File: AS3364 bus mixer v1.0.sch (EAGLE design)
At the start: 93 parts, among them IC1 TL072JT, IC2 TL072JT, IC3 TL072JT, IC30 TL072JT, IC4 TL072JT, IC5 79L09F, IC6 78L09F, IC7 CH446Q

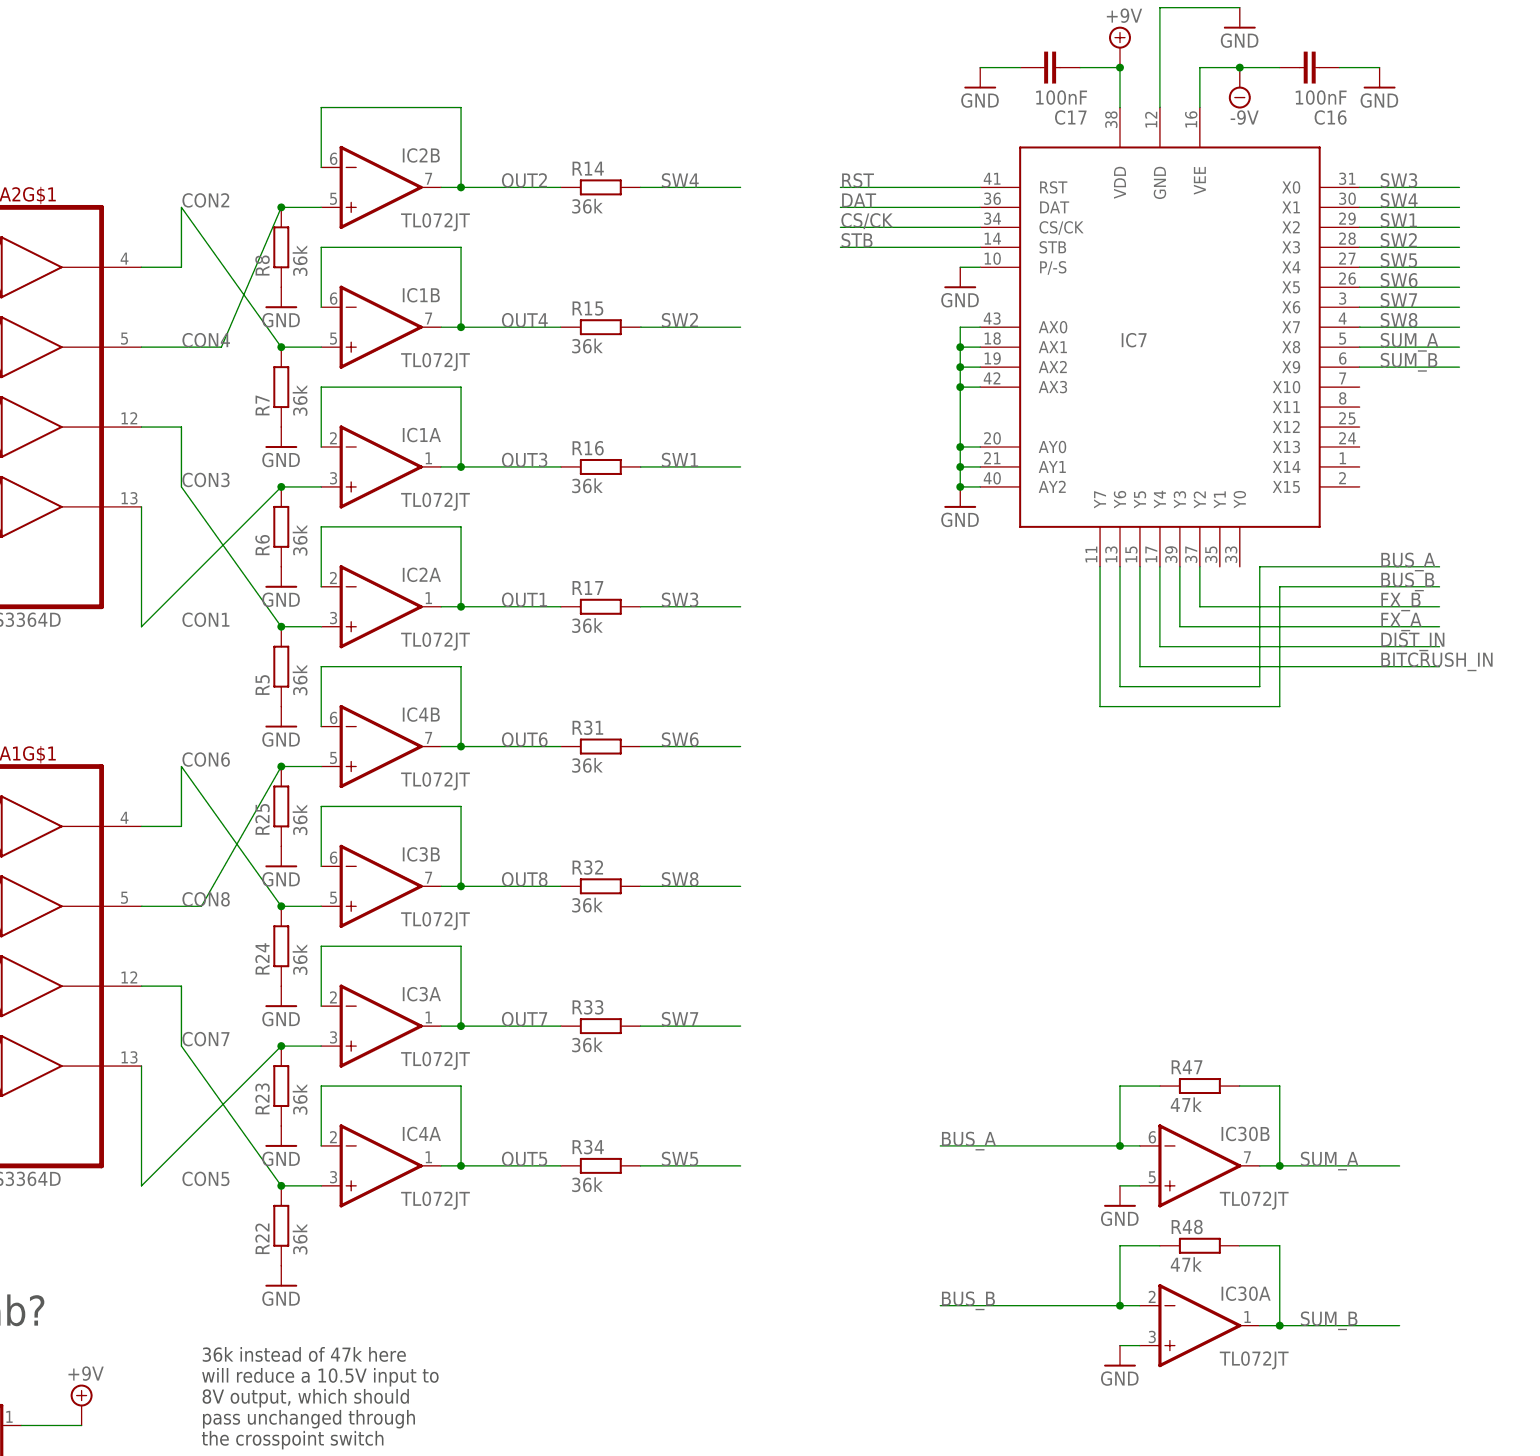
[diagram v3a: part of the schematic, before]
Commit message: Reordered lines to make coding easier
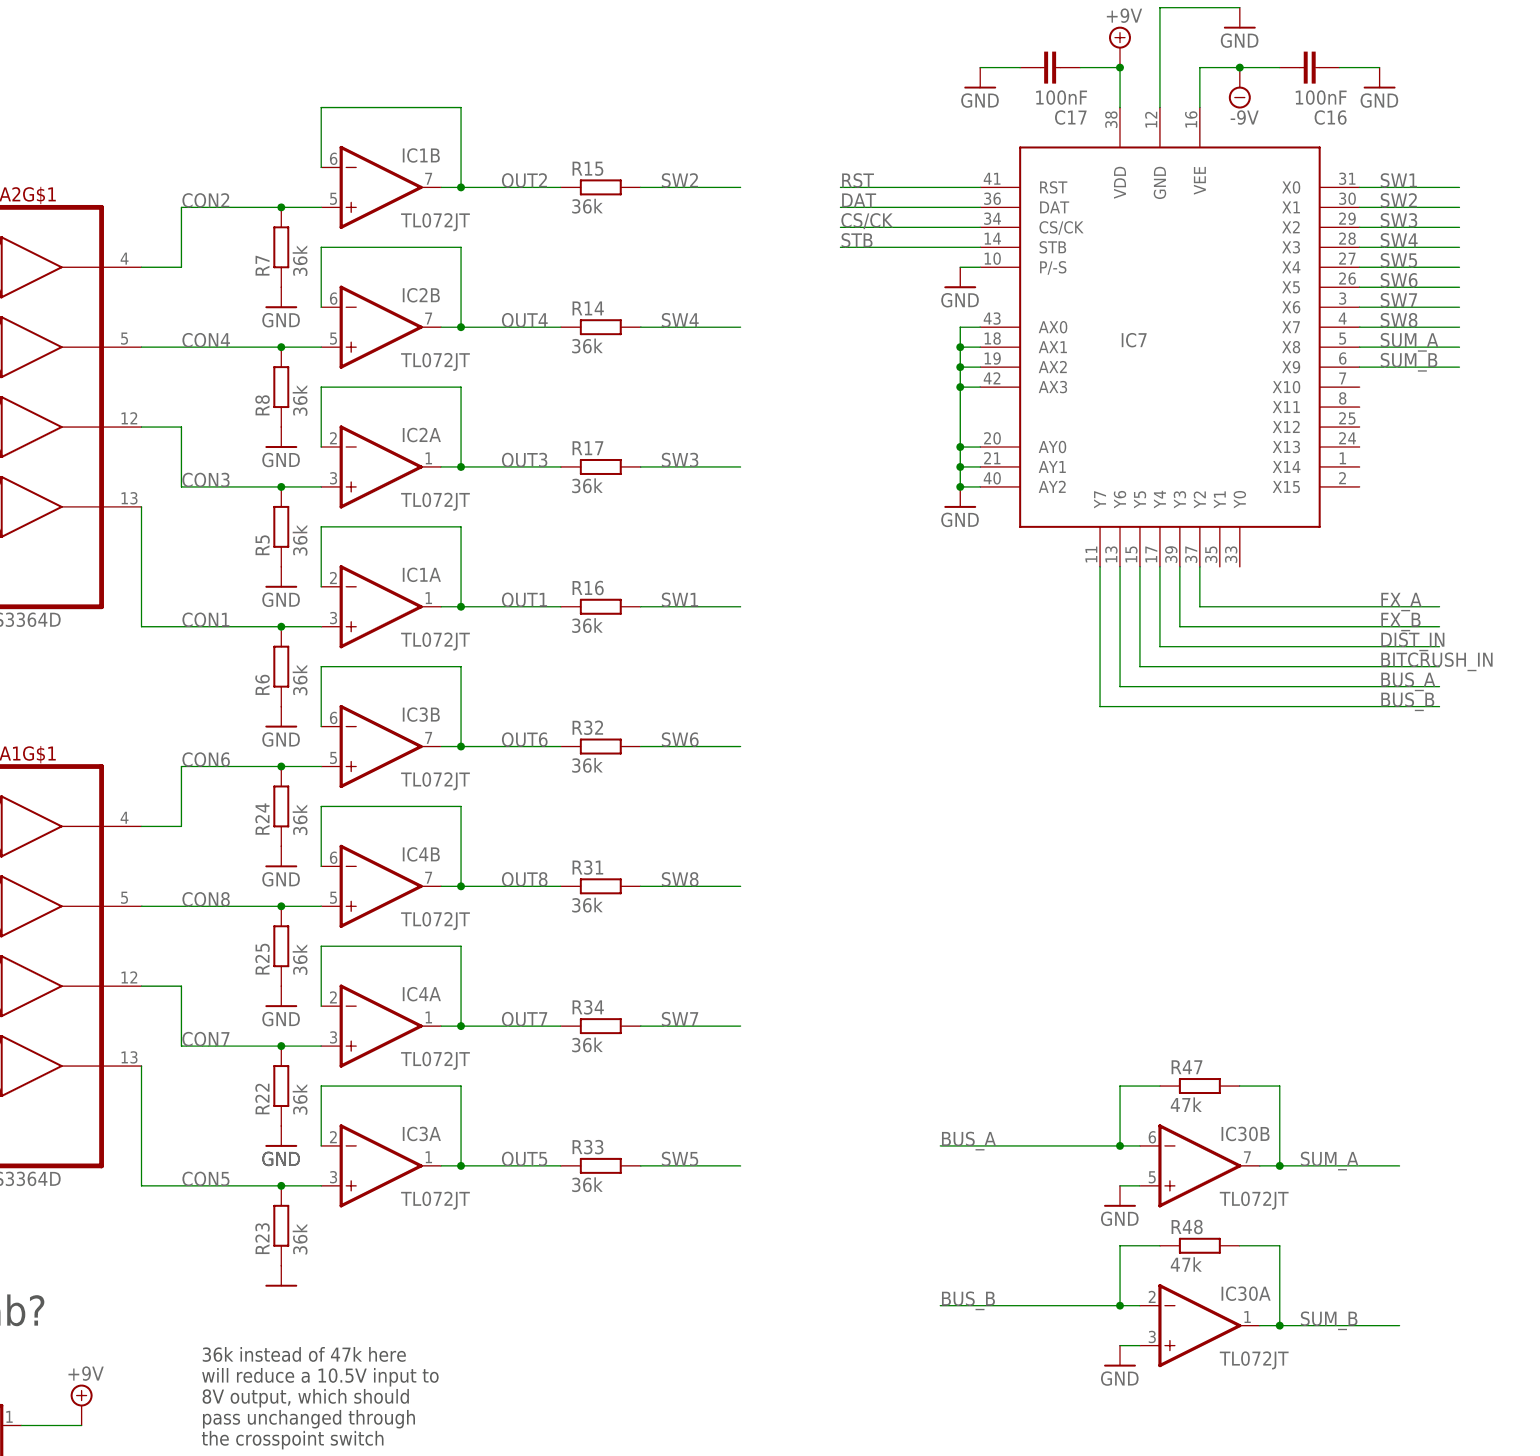
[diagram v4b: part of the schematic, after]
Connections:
- net FX_A: now also IC7.Y2; no longer IC7.Y3
- net FX_B: now also IC7.Y3; no longer IC7.Y2
- net OUT1: now also IC1A.-IN, IC1A.OUT, R16.1; no longer IC2A.-IN, IC2A.OUT, R17.1
- net OUT2: now also IC1B.-IN, IC1B.OUT, R15.1; no longer IC2B.-IN, IC2B.OUT, R14.1
- net OUT3: now also IC2A.-IN, IC2A.OUT, R17.1; no longer IC1A.-IN, IC1A.OUT, R16.1
- net OUT4: now also IC2B.-IN, IC2B.OUT, R14.1; no longer IC1B.-IN, IC1B.OUT, R15.1
- net OUT5: now also IC3A.-IN, IC3A.OUT, R33.1; no longer IC4A.-IN, IC4A.OUT, R34.1
- net OUT6: now also IC3B.-IN, IC3B.OUT, R32.1; no longer IC4B.-IN, IC4B.OUT, R31.1
- net OUT7: now also IC4A.-IN, IC4A.OUT, R34.1; no longer IC3A.-IN, IC3A.OUT, R33.1
- net OUT8: now also IC4B.-IN, IC4B.OUT, R31.1; no longer IC3B.-IN, IC3B.OUT, R32.1
- net SW1: now also IC7.X0; no longer IC7.X2
- net SW2: now also IC7.X1; no longer IC7.X3
- net SW3: now also IC7.X2; no longer IC7.X0
- net SW4: now also IC7.X3; no longer IC7.X1
- net SW5: now also R33.2; no longer R34.2
- net SW6: now also R32.2; no longer R31.2
- net SW7: now also R34.2; no longer R33.2
- net SW8: now also R31.2; no longer R32.2
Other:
- moved on the sheet: IC1A, IC1B, IC2A, IC2B, IC3A, IC3B, IC4A, IC4B, R14, R15, R16, R17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

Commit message: Added 220k resistors to bus
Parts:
- added R35, R36: 220k, rcl:R-EU_R0402
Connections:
- net BUS_A: now also R35.2
- net BUS_B: now also R36.2
- net GND: now also R35.1, R36.1
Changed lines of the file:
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@@
 <part name="GND27" library="supply1" library_urn="urn:adsk.eagle:library:371" deviceset="GND" device=""/>
 <part name="GND28" library="supply1" library_urn="urn:adsk.eagle:library:371" deviceset="GND" device=""/>
+<part name="R35" library="rcl" library_urn="urn:adsk.eagle:library:334" deviceset="R-EU_" device="R0402" package3d_urn="urn:adsk.eagle:package:23547/3" value="220k"/>
+<part name="R36" library="rcl" library_urn="urn:adsk.eagle:library:334" deviceset="R-EU_" device="R0402" package3d_urn="urn:adsk.eagle:package:23547/3" value="220k"/>
+<part name="GND29" library="supply1" library_urn="urn:adsk.eagle:library:371" deviceset="GND" device=""/>
+<part name="GND30" library="supply1" library_urn="urn:adsk.eagle:library:371" deviceset="GND" device=""/>
 </parts>
 <sheets>
@@
 <instance part="GND28" gate="1" x="198.12" y="-68.58" smashed="yes">
 <attribute name="VALUE" x="195.58" y="-71.12" size="1.778" layer="96"/>
+</instance>
+<instance part="R35" gate="G$1" x="180.34" y="-45.72" smashed="yes">
+<attribute name="NAME" x="176.53" y="-44.2214" size="1.778" layer="95"/>
+<attribute name="VALUE" x="176.53" y="-49.022" size="1.778" layer="96"/>
+</instance>
+<instance part="R36" gate="G$1" x="180.34" y="-66.04" smashed="yes">
+<attribute name="NAME" x="176.53" y="-64.5414" size="1.778" layer="95"/>
+<attribute name="VALUE" x="176.53" y="-69.342" size="1.778" layer="96"/>
+</instance>
+<instance part="GND29" gate="1" x="172.72" y="-48.26" smashed="yes">
+<attribute name="VALUE" x="170.18" y="-50.8" size="1.778" layer="96"/>
+</instance>
+<instance part="GND30" gate="1" x="172.72" y="-68.58" smashed="yes">
+<attribute name="VALUE" x="170.18" y="-71.12" size="1.778" layer="96"/>
 </instance>
 </instances>
@@
 <wire x1="198.12" y1="-66.04" x2="200.66" y2="-66.04" width="0.1524" layer="91"/>
 <pinref part="GND28" gate="1" pin="GND"/>
+</segment>
+<segment>
+<pinref part="R35" gate="G$1" pin="1"/>
+<pinref part="GND29" gate="1" pin="GND"/>
+<wire x1="175.26" y1="-45.72" x2="172.72" y2="-45.72" width="0.1524" layer="91"/>
+</segment>
+<segment>
+<pinref part="R36" gate="G$1" pin="1"/>
+<pinref part="GND30" gate="1" pin="GND"/>
+<wire x1="175.26" y1="-66.04" x2="172.72" y2="-66.04" width="0.1524" layer="91"/>
 </segment>
 </net>
@@
 <pinref part="R48" gate="G$1" pin="1"/>
 <wire x1="198.12" y1="-53.34" x2="203.2" y2="-53.34" width="0.1524" layer="91"/>
-<wire x1="175.26" y1="-60.96" x2="198.12" y2="-60.96" width="0.1524" layer="91"/>
+<wire x1="175.26" y1="-60.96" x2="193.04" y2="-60.96" width="0.1524" layer="91"/>
 <junction x="198.12" y="-60.96"/>
 <label x="175.26" y="-60.96" size="1.778" layer="95"/>
+<pinref part="R36" gate="G$1" pin="2"/>
+<wire x1="193.04" y1="-60.96" x2="198.12" y2="-60.96" width="0.1524" layer="91"/>
+<wire x1="185.42" y1="-66.04" x2="193.04" y2="-66.04" width="0.1524" layer="91"/>
+<wire x1="193.04" y1="-66.04" x2="193.04" y2="-60.96" width="0.1524" layer="91"/>
+<junction x="193.04" y="-60.96"/>
 </segment>
 <segment>
@@
 <wire x1="198.12" y1="-33.02" x2="203.2" y2="-33.02" width="0.1524" layer="91"/>
 <junction x="198.12" y="-40.64"/>
-<wire x1="198.12" y1="-40.64" x2="175.26" y2="-40.64" width="0.1524" layer="91"/>
+<wire x1="198.12" y1="-40.64" x2="193.04" y2="-40.64" width="0.1524" layer="91"/>
 <label x="175.26" y="-40.64" size="1.778" layer="95"/>
-</segment>
-<segment>
+<pinref part="R35" gate="G$1" pin="2"/>
+<wire x1="193.04" y1="-40.64" x2="175.26" y2="-40.64" width="0.1524" layer="91"/>
+<wire x1="185.42" y1="-45.72" x2="193.04" y2="-45.72" width="0.1524" layer="91"/>
+<wire x1="193.04" y1="-45.72" x2="193.04" y2="-40.64" width="0.1524" layer="91"/>
+<junction x="193.04" y="-40.64"/>
+</segment>
+<segment>

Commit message: Switched to 16x2 connector
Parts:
- removed +12V, -12V, BC_IN, BUS_A, BUS_B, CS/CK, CV1, CV2, CV3, CV4, CV5, CV6, CV7, CV8, DAT, DIST_IN, FX_A, FX_B, GND, IN1, IN2, IN3, IN4, IN5, IN6, IN7, IN8, RST, STB, STB1, STB2, STB3: (no value), joakim:MA01-1JN8MM
- added SV1: (no value), joakim:MA16-2WJ
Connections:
- net +12V: now also SV1.18; no longer +12V.1
- net -12V: now also SV1.15; no longer -12V.1
- net BITCRUSH_IN: now also SV1.13; no longer BC_IN.1
- net BUS_A: now also SV1.4; no longer BUS_A.1
- net BUS_B: now also SV1.2; no longer BUS_B.1
- net CS/CK: now also SV1.31; no longer CS/CK.1
- net CV1: now also SV1.26; no longer CV1.1
- net CV2: now also SV1.24; no longer CV2.1
- net CV3: now also SV1.22; no longer CV3.1
- net CV4: now also SV1.20; no longer CV4.1
- net CV5: now also SV1.12; no longer CV5.1
- net CV6: now also SV1.10; no longer CV6.1
- net CV7: now also SV1.8; no longer CV7.1
- net CV8: now also SV1.6; no longer CV8.1
- net DAT: now also SV1.32; no longer DAT.1
- net DIST_IN: now also SV1.14; no longer DIST_IN.1
- net FX_A: now also SV1.3; no longer FX_A.1
- net FX_B: now also SV1.1; no longer FX_B.1
- net GND: now also SV1.17; no longer GND.1
- net IN1: now also SV1.25; no longer IN1.1
- net IN2: now also SV1.23; no longer IN2.1
- net IN3: now also SV1.21; no longer IN3.1
- net IN4: now also SV1.19; no longer IN4.1
- net IN5: now also SV1.11; no longer IN5.1
- net IN6: now also SV1.9; no longer IN6.1
- net IN7: now also SV1.7; no longer IN7.1
- net IN8: now also SV1.5; no longer IN8.1
- net RST: now also SV1.29; no longer RST.1
- net STB: now also SV1.30; no longer STB.1
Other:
- note removed: "TODO: Change gain resistors"
- note removed: "TODO: Connect tab?"
- moved on the sheet: IC5
